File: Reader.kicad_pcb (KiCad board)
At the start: 2 copper layers, 40.4 x 60 mm, 41 parts, among them J1 Conn_01x04, J2 Amphenol Dubox ‎76383-402LF‎, J3 Conn_01x04, J4 Conn_01x08, J5 Conn_01x10, J6 Conn_01x03, J7 Conn_01x02, Q1 2N7002, Q2 2N7002, Q3 2N7002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

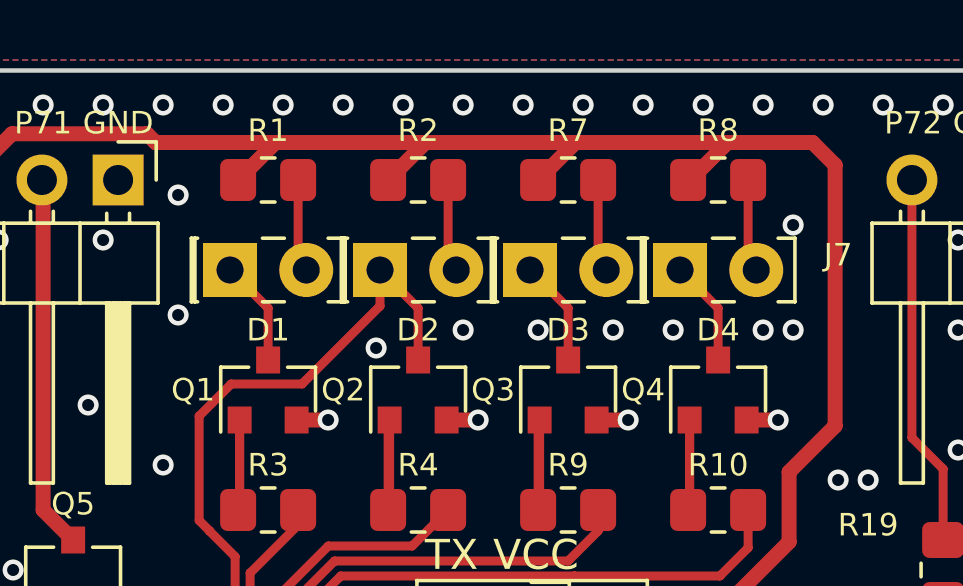
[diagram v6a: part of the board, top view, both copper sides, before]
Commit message: Mark LED polarity on silkscreen
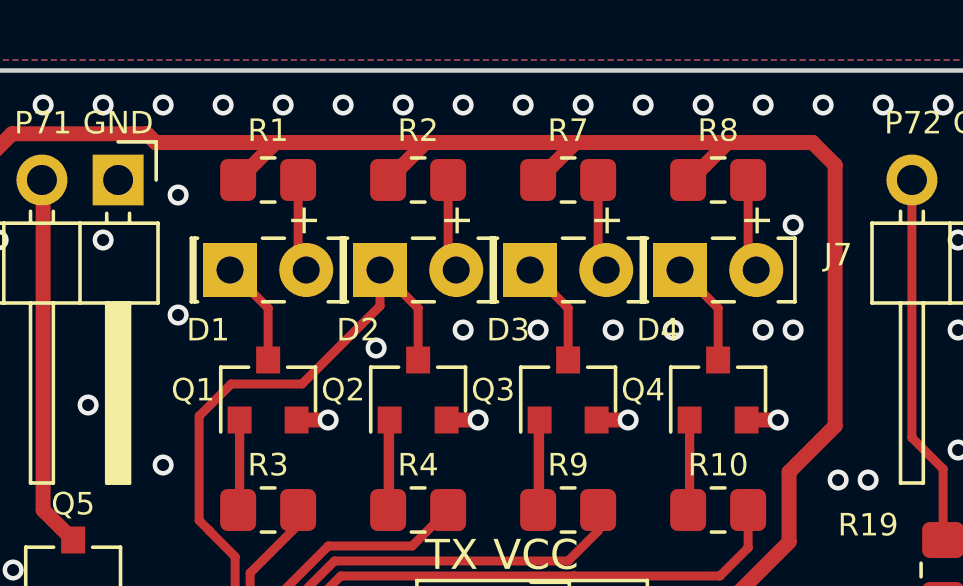
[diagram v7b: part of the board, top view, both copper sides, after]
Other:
- board text added: "+"
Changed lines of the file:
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@@
     (property "ki_keywords" "LED diode")
     (attr through_hole)
-    (fp_text reference "D3" (at 1.27 2) (layer "F.SilkS")
+    (fp_text reference "D3" (at -0.73 2) (layer "F.SilkS")
         (effects (font (size 0.75 0.75) (thickness 0.1)))
     )
@@
     (property "ki_keywords" "LED diode")
     (attr through_hole)
-    (fp_text reference "D1" (at 1.27 2) (layer "F.SilkS")
+    (fp_text reference "D1" (at -0.73 2) (layer "F.SilkS")
         (effects (font (size 0.75 0.75) (thickness 0.1)))
     )
@@
     (property "ki_keywords" "LED diode")
     (attr through_hole)
-    (fp_text reference "D2" (at 1.27 2) (layer "F.SilkS")
+    (fp_text reference "D2" (at -0.73 2) (layer "F.SilkS")
         (effects (font (size 0.75 0.75) (thickness 0.1)))
     )
@@
     (property "ki_keywords" "LED diode")
     (attr through_hole)
-    (fp_text reference "D4" (at 1.27 2) (layer "F.SilkS")
+    (fp_text reference "D4" (at -0.73 2) (layer "F.SilkS")
         (effects (font (size 0.75 0.75) (thickness 0.1)))
     )
@@
     (effects (font (size 1 1) (thickness 0.15)))
   )
+  (gr_text "+" (at 108.8 66.9) (layer "F.SilkS")
+    (effects (font (size 1 1) (thickness 0.15)) (justify bottom))
+  )
   (gr_text "GND" (at 102.5 82.5) (layer "F.SilkS")
     (effects (font (size 1 1) (thickness 0.15)) (justify left))
   )
+  (gr_text "+" (at 103.8 66.9) (layer "F.SilkS")
+    (effects (font (size 1 1) (thickness 0.15)) (justify bottom))
+  )
+  (gr_text "+" (at 98.8 66.9) (layer "F.SilkS")
+    (effects (font (size 1 1) (thickness 0.15)) (justify bottom))
+  )
+  (gr_text "+" (at 93.7 66.9) (layer "F.SilkS")
+    (effects (font (size 1 1) (thickness 0.15)) (justify bottom))
+  )
   (gr_text "Plug ends here" (at 100 99.5) (layer "Dwgs.User")

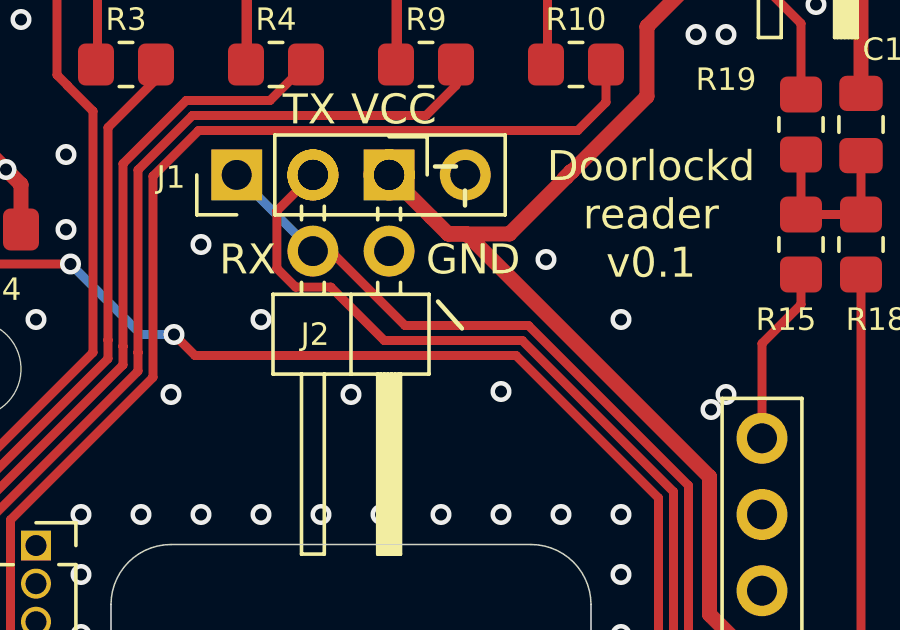
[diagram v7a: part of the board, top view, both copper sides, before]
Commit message: Remove unintended silkscreen line
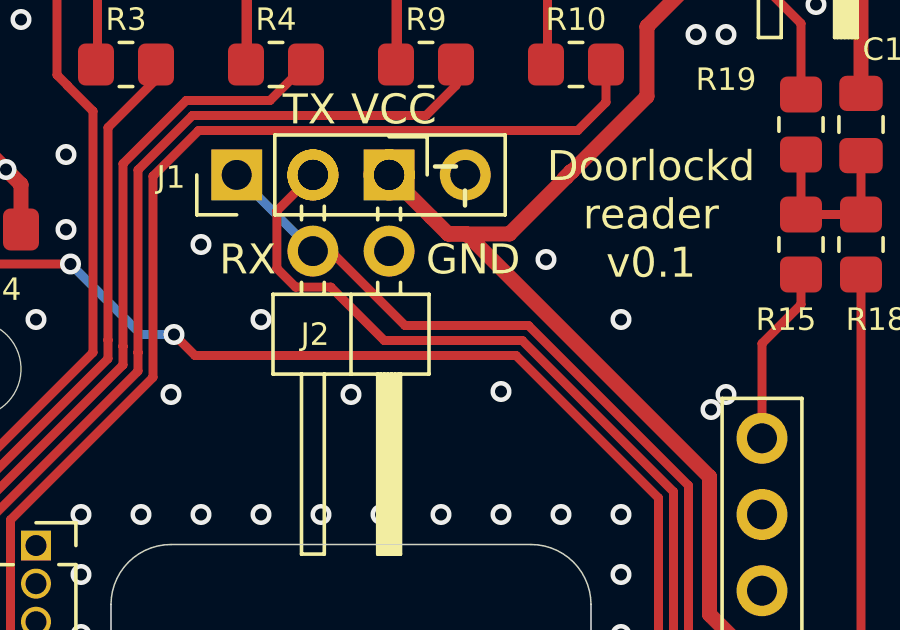
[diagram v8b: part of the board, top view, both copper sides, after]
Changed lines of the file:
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@@
     )
   )
-  (gr_line (start 103.7 84.8) (end 102.9 83.9)
-    (stroke (width 0.15) (type solid)) (layer "F.SilkS"))
   (gr_line (start 103.5 79.4) (end 102.8 79.4)
     (stroke (width 0.15) (type solid)) (layer "F.SilkS"))
